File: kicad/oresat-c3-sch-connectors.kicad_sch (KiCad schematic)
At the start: 26 parts, among them J1 J-SAMTEC-TFM-120-01-L-D-RA, J3 J-TE-Debug-2-1734592-0

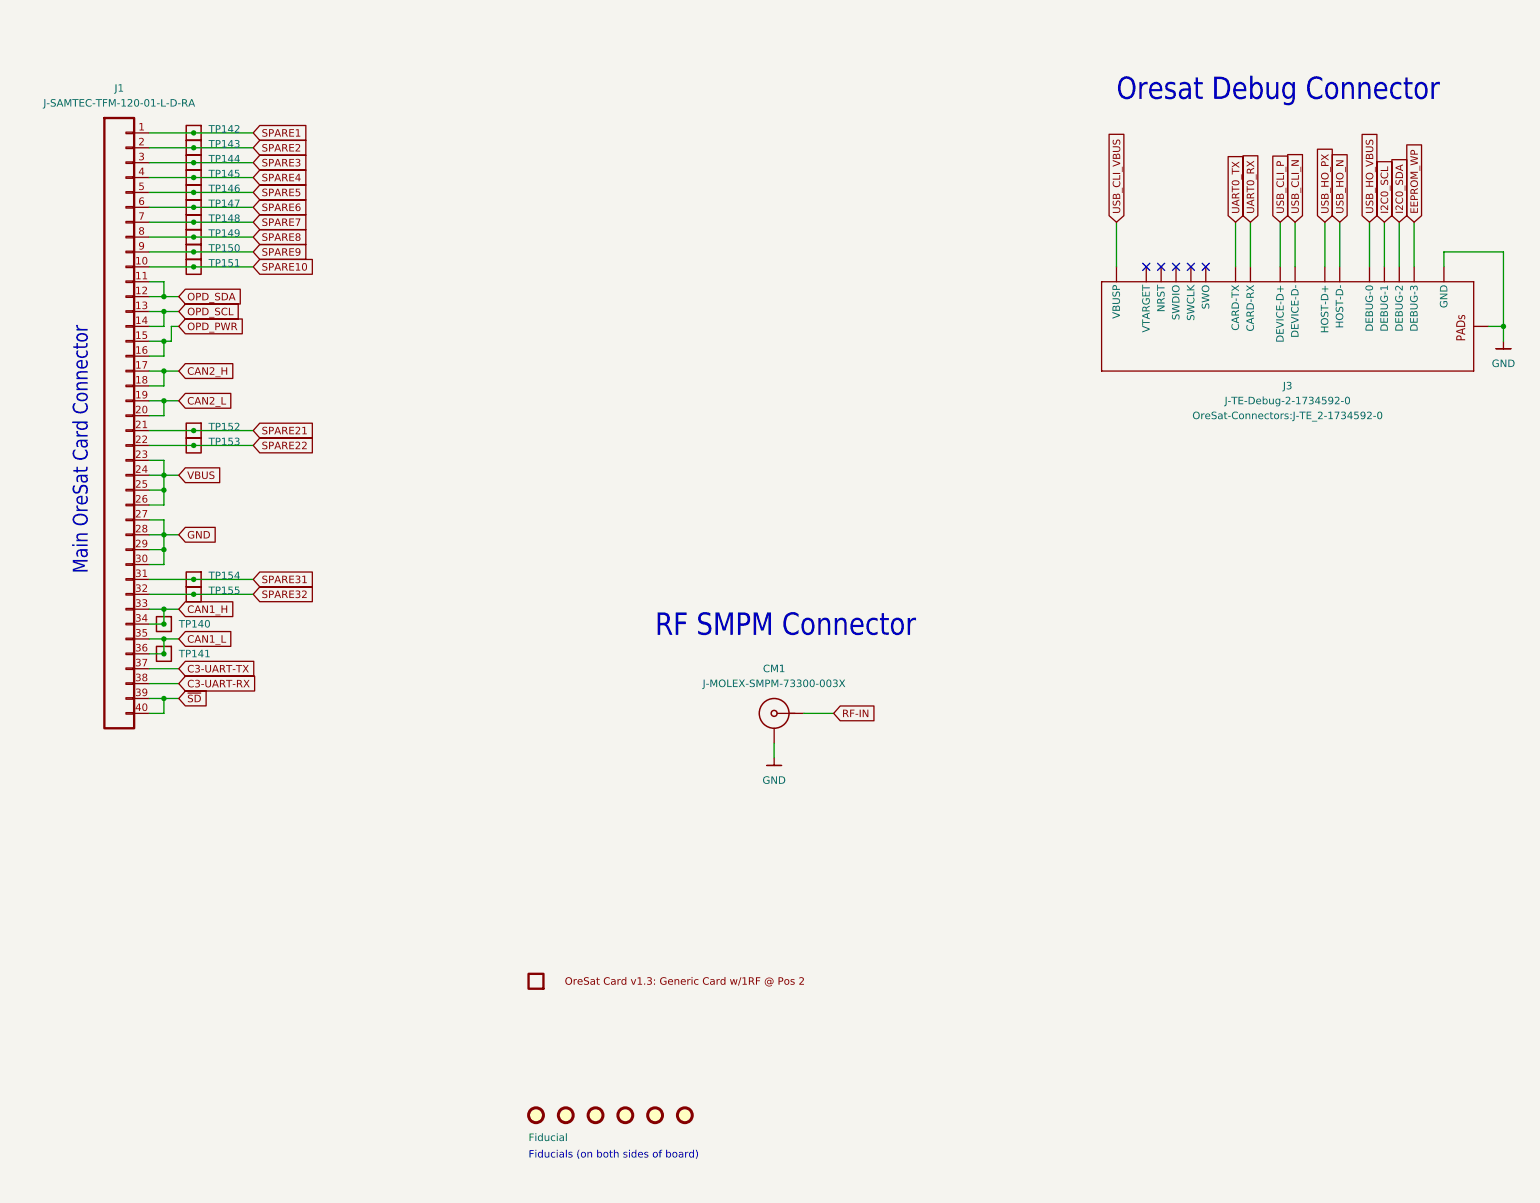
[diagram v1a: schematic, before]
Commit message: C3 v6 schematic now 80% done. OSD2258 IC has been gone over with a fine tooth comb and simplified as much as possible. OSD3358 pinout compared to RED board and PocketBeagle. What's left: lots of little issues, footprints, and then L band and UHF radio schematics need to be fixed.
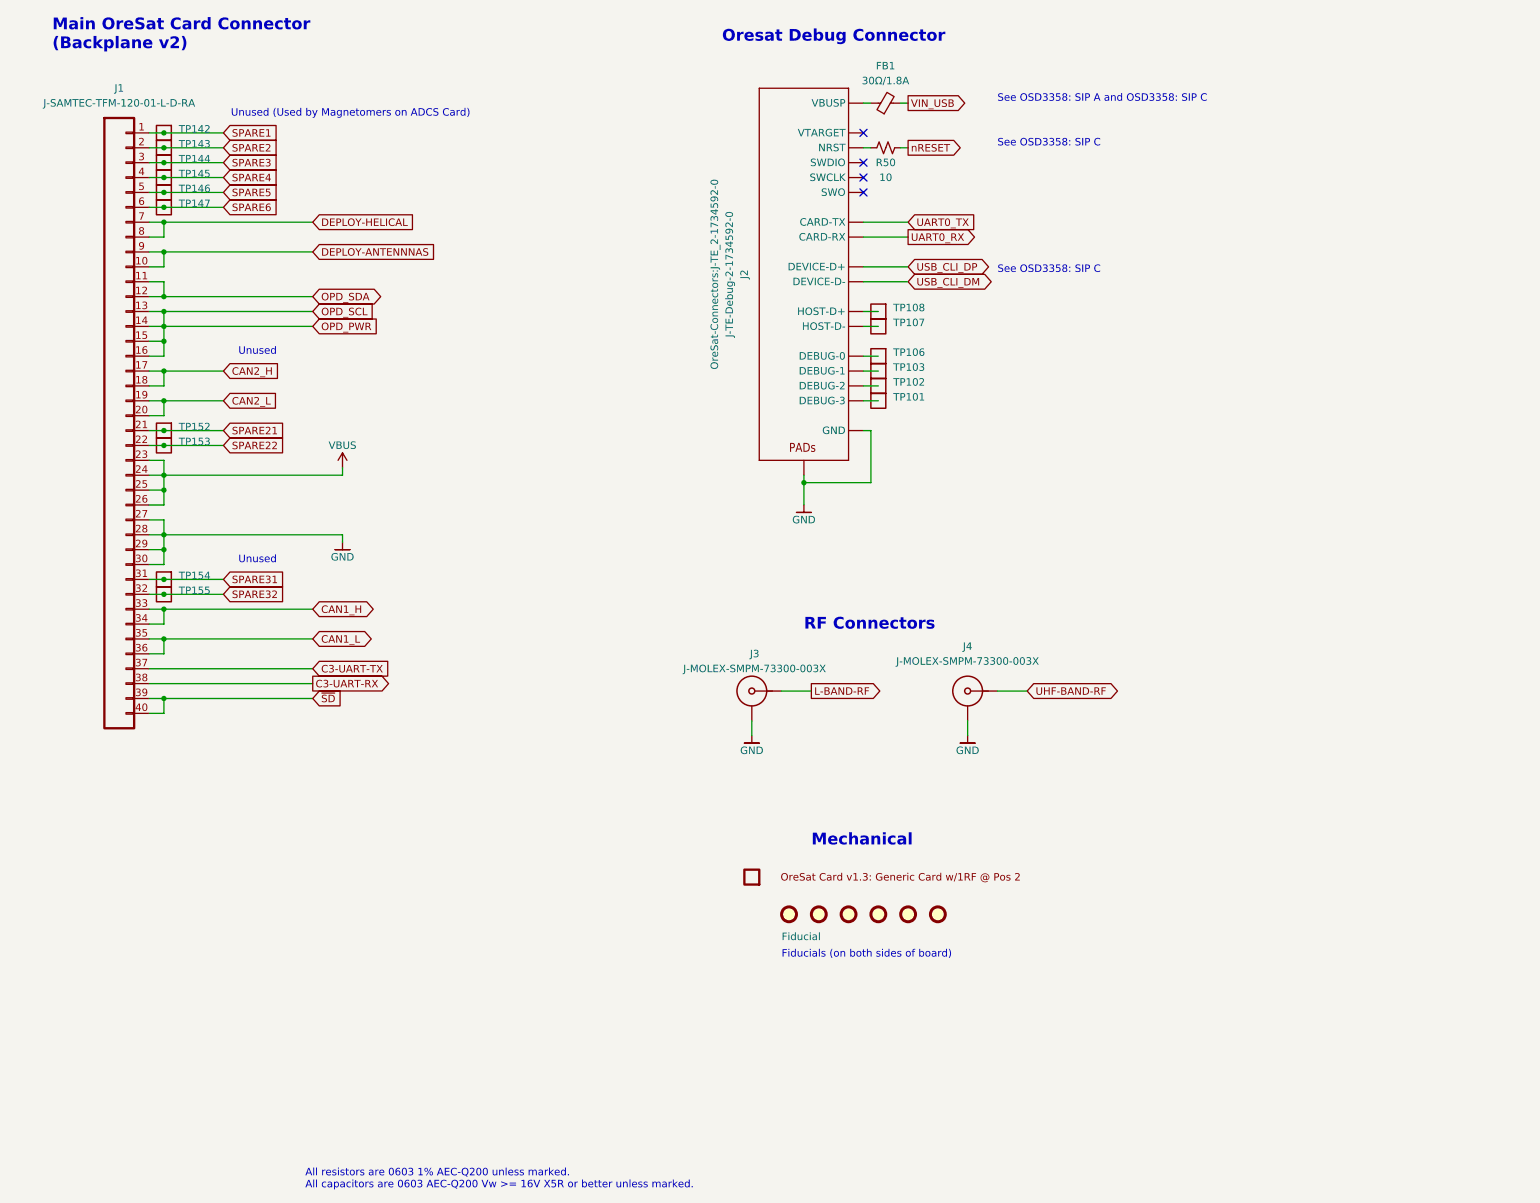
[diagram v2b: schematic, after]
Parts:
- removed TP140, TP141, TP148, TP149, TP150, TP151: Test-Point, OreSat-TestPoint:PAD.03X.04, symbol OreSat-TestPoint:Test-Point
- added FB1: 30Ω/1.8A, Inductor_SMD:L_0603_1608Metric, symbol Device:FerriteBead_Small
- added J4: J-MOLEX-SMPM-73300-003X, oresat-connectors:J-MOLEX-SMPM-073300-003X, symbol oresat-connectors:J-MOLEX-SMPM-73300-003X
- added R50: 10, Resistor_SMD:R_0603_1608Metric, symbol Device:R_Small_US
- added TP101, TP102, TP103, TP106, TP107, TP108: Test-Point, OreSat-TestPoint:PAD.03X.04, symbol OreSat-TestPoint:Test-Point
- J3: renamed from CM1; footprint oresat-footprints:J-MOLEX-SMPM-073300-003X -> oresat-connectors:J-MOLEX-SMPM-073300-003X; symbol j-molex-smpm-73300-003x:J-MOLEX-SMPM-73300-003X -> oresat-connectors:J-MOLEX-SMPM-73300-003X
- renumbered J3 to J2
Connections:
- net OPD_SCL is gone; now on net OPD_PWR: J1.13, J1.14
- net SPARE8 is gone; now on net DEPLOY-HELICAL: J1.8
- net SPARE9 is gone; now on net DEPLOY-ANTENNNAS: J1.9
- net GND: now also J4.GND (SHIELD3)
- net at J2.10 (NRST): now also R50.1
- net EEPROM_WP: no longer names the net of J2.20 (DEBUG-3)
- net EEPROM_WP: now also TP101.1
- net I2C0_SCL: no longer names the net of J2.18 (DEBUG-1)
- net I2C0_SCL: now also TP103.1
- net I2C0_SDA: no longer names the net of J2.19 (DEBUG-2)
- net I2C0_SDA: now also TP102.1
- net RF-IN renamed L-BAND-RF
- net SPARE10 renamed DEPLOY-ANTENNNAS
- net SPARE7 renamed DEPLOY-HELICAL
- net USB_CLI_N renamed USB_CLI_DM
- net USB_CLI_P renamed USB_CLI_DP
- net USB_CLI_VBUS: no longer names the net of J2.1 (VBUSP), J2.2 (VBUSP)
- net USB_CLI_VBUS: now also FB1.1
- net USB_HO_N: no longer names the net of J2.8 (HOST-D-)
- net USB_HO_N: now also TP107.1
- net USB_HO_PX: no longer names the net of J2.7 (HOST-D+)
- net USB_HO_PX: now also TP108.1
- net USB_HO_VBUS: no longer names the net of J2.17 (DEBUG-0)
- net USB_HO_VBUS: now also TP106.1
- new net UHF-BAND-RF: J4.RF (CENTER)
- new net VIN_USB: FB1.2
- new net nRESET: R50.2
- no-connect marks 5 -> 4
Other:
- note added: "All resistors are 0603 1% AEC-Q200 unless marked. All capacitors are 0603 AEC-Q200 Vw >= 16V X5R or better unless marked."
- note added: "Main OreSat Card Connector (Backplane v2)"
- note added: "Mechanical"
- note added: "RF Connectors"
- note added: "See OSD3358: SIP A and OSD3358: SIP C"
- note added: "See OSD3358: SIP C"
- note added: "Unused"
- note added: "Unused (Used by Magnetomers on ADCS Card)"
- note removed: "Main OreSat Card Connector"
- note removed: "RF SMPM Connector"
- title: (none) -> OreSat C3: Connectors
- moved on the sheet: J2, J3, TP142, TP143, TP144, TP145, TP146, TP147, TP152, TP153, TP154, TP155
